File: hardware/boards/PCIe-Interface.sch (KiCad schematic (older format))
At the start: 1 part, among them U1 ECP5UM5G-381caBGA

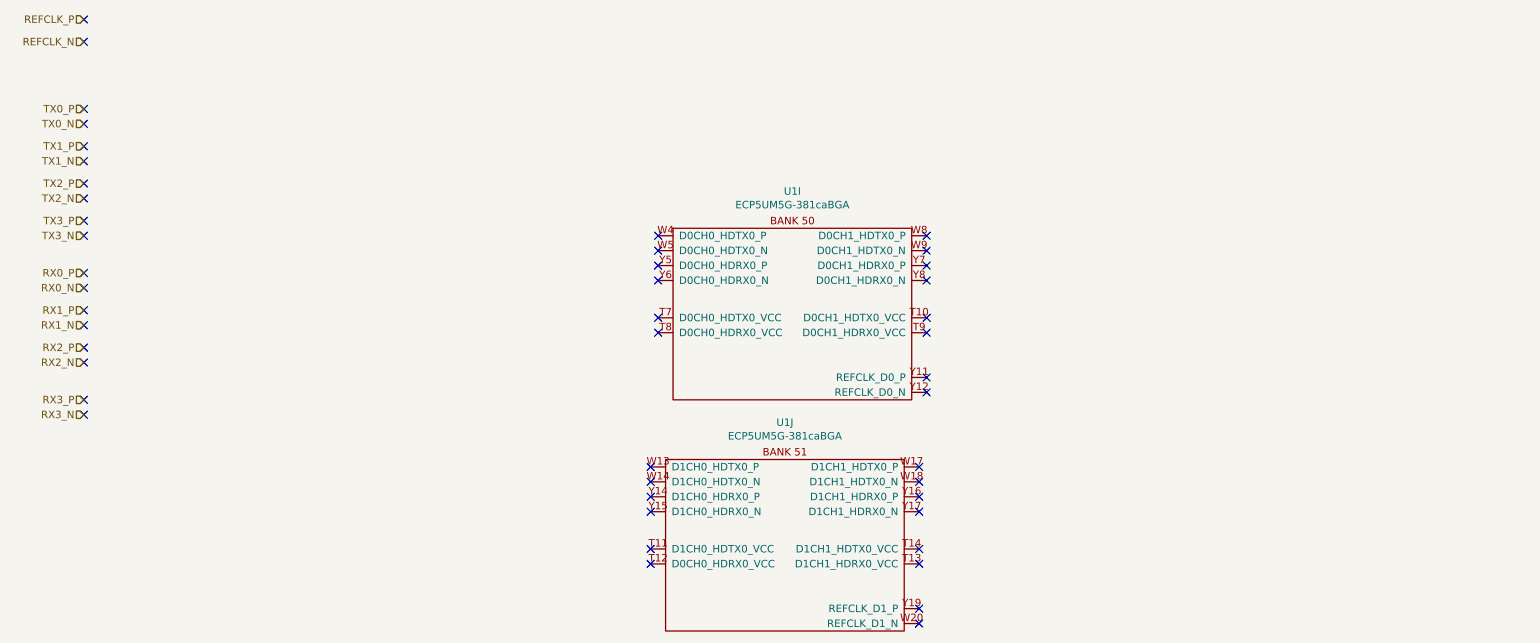
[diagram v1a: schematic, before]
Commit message: Added a clock fanout buffer for the PCIe REFCLOCK to connect to the FPGAs SERDES banks
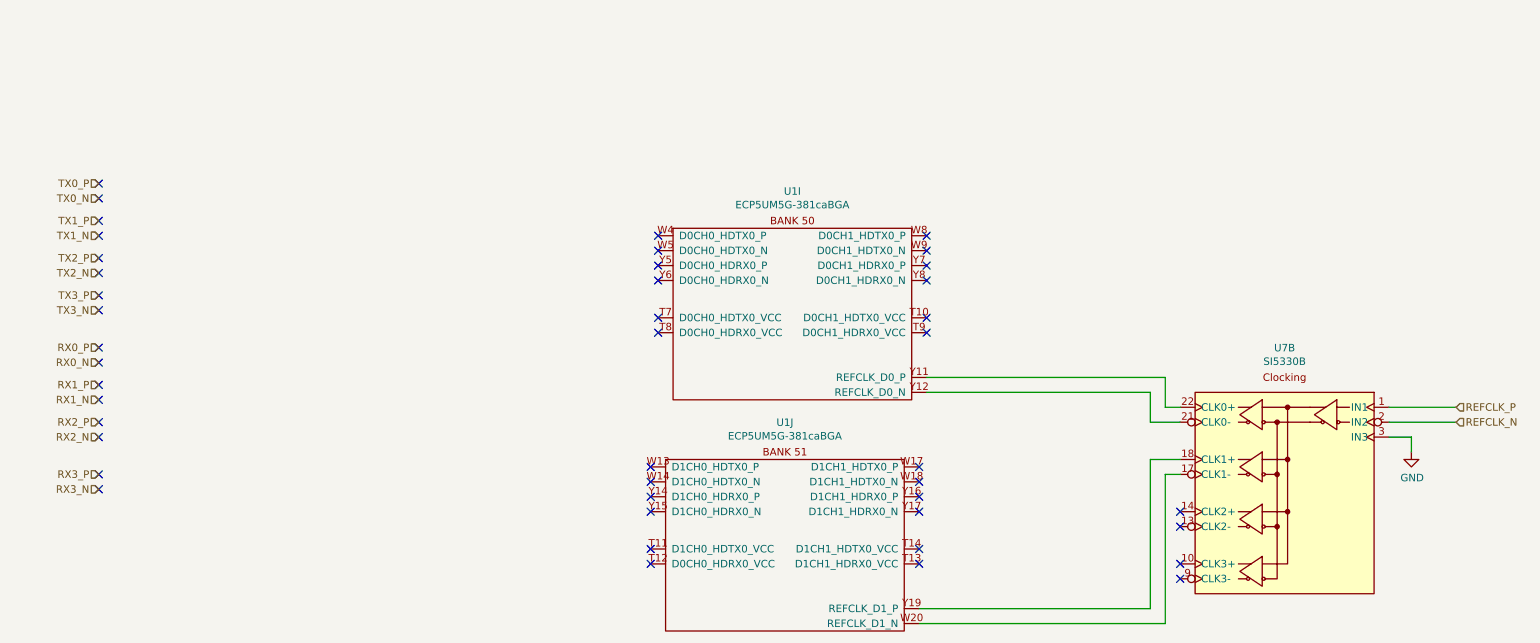
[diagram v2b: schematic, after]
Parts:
- added U7: SI5330B, Package_DFN_QFN:VQFN-24-1EP_4x4mm_P0.5mm_EP2.45x2.45mm, symbol lethalbit:SI5330B
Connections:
- net REFCLK_N: now also U7.2 (IN2)
- net REFCLK_P: now also U7.1 (IN1)
- net at U1.Y11 (REFCLK_D0_P): now also U7.22 (CLK0+)
- net at U1.Y12 (REFCLK_D0_N): now also U7.21 (CLK0-)
- net at U1.W20 (REFCLK_D1_N): now also U7.17 (CLK1-)
- net at U1.Y19 (REFCLK_D1_P): now also U7.18 (CLK1+)
- new net GND: U7.3 (IN3)
- no-connect marks 46 -> 44
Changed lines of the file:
@@
 Comment4 ""
 $EndDescr
-Text HLabel 1300 800  0    50   Input ~ 0
+Text HLabel 10500 3400 2    50   Input ~ 0
 REFCLK_P
-Text HLabel 1300 950  0    50   Input ~ 0
+Text HLabel 10500 3500 2    50   Input ~ 0
 REFCLK_N
-Text HLabel 1300 1400 0    50   Input ~ 0
+Text HLabel 1400 1900 0    50   Input ~ 0
 TX0_P
-Text HLabel 1300 1500 0    50   Input ~ 0
+Text HLabel 1400 2000 0    50   Input ~ 0
 TX0_N
-Text HLabel 1300 1650 0    50   Input ~ 0
+Text HLabel 1400 2150 0    50   Input ~ 0
 TX1_P
-Text HLabel 1300 1750 0    50   Input ~ 0
+Text HLabel 1400 2250 0    50   Input ~ 0
 TX1_N
-Text HLabel 1300 1900 0    50   Input ~ 0
+Text HLabel 1400 2400 0    50   Input ~ 0
 TX2_P
-Text HLabel 1300 2000 0    50   Input ~ 0
+Text HLabel 1400 2500 0    50   Input ~ 0
 TX2_N
-Text HLabel 1300 2150 0    50   Input ~ 0
+Text HLabel 1400 2650 0    50   Input ~ 0
 TX3_P
-Text HLabel 1300 2250 0    50   Input ~ 0
+Text HLabel 1400 2750 0    50   Input ~ 0
 TX3_N
-Text HLabel 1300 2500 0    50   Input ~ 0
+Text HLabel 1400 3000 0    50   Input ~ 0
 RX0_P
-Text HLabel 1300 2600 0    50   Input ~ 0
+Text HLabel 1400 3100 0    50   Input ~ 0
 RX0_N
-Text HLabel 1300 2750 0    50   Input ~ 0
+Text HLabel 1400 3250 0    50   Input ~ 0
 RX1_P
-Text HLabel 1300 2850 0    50   Input ~ 0
+Text HLabel 1400 3350 0    50   Input ~ 0
 RX1_N
-Text HLabel 1300 3000 0    50   Input ~ 0
+Text HLabel 1400 3500 0    50   Input ~ 0
 RX2_P
-Text HLabel 1300 3100 0    50   Input ~ 0
+Text HLabel 1400 3600 0    50   Input ~ 0
 RX2_N
-Text HLabel 1300 3350 0    50   Input ~ 0
+Text HLabel 1400 3850 0    50   Input ~ 0
 RX3_P
-Text HLabel 1300 3450 0    50   Input ~ 0
+Text HLabel 1400 3950 0    50   Input ~ 0
 RX3_N
 $Comp
@@
 	1    0    0    -1
 $EndComp
-NoConn ~ 1300 800
-NoConn ~ 1300 950
-NoConn ~ 1300 1400
-NoConn ~ 1300 1500
-NoConn ~ 1300 1650
-NoConn ~ 1300 1750
-NoConn ~ 1300 1900
-NoConn ~ 1300 2000
-NoConn ~ 1300 2150
-NoConn ~ 1300 2250
-NoConn ~ 1300 2500
-NoConn ~ 1300 2600
-NoConn ~ 1300 2750
-NoConn ~ 1300 2850
-NoConn ~ 1300 3000
-NoConn ~ 1300 3100
-NoConn ~ 1300 3350
-NoConn ~ 1300 3450
+NoConn ~ 1400 1900
+NoConn ~ 1400 2000
+NoConn ~ 1400 2150
+NoConn ~ 1400 2250
+NoConn ~ 1400 2400
+NoConn ~ 1400 2500
+NoConn ~ 1400 2650
+NoConn ~ 1400 2750
+NoConn ~ 1400 3000
+NoConn ~ 1400 3100
+NoConn ~ 1400 3250
+NoConn ~ 1400 3350
+NoConn ~ 1400 3500
+NoConn ~ 1400 3600
+NoConn ~ 1400 3850
+NoConn ~ 1400 3950
 NoConn ~ 5150 2250
 NoConn ~ 5150 2350
@@
 NoConn ~ 6900 4350
 NoConn ~ 6900 4450
-NoConn ~ 6900 4750
-NoConn ~ 6900 4850
-NoConn ~ 6950 3300
-NoConn ~ 6950 3200
 NoConn ~ 6950 2900
 NoConn ~ 6950 2800
@@
 NoConn ~ 6950 2350
 NoConn ~ 6950 2250
+$Comp
+L lethalbit:SI5330B U7
+U 2 1 5F1A1842
+P 9350 3400
+F 0 "U7" H 9350 3798 50  0000 C CNN
+F 1 "SI5330B" H 9350 3707 50  0000 C CNN
+F 2 "Package_DFN_QFN:VQFN-24-1EP_4x4mm_P0.5mm_EP2.45x2.45mm" H 9350 3700 50  0001 C CNN
+F 3 "https://www.silabs.com/documents/public/data-sheets/Si5330.pdf" H 9350 3700 50  0001 C CNN
+F 4 "Silicon Labs" H 9350 3400 50  0001 C CNN "MFR"
+F 5 "SI5330B-B00205-GM" H 9350 3400 50  0001 C CNN "MPN"
+	2    9350 3400
+	-1   0    0    -1
+$EndComp
+Wire Wire Line
+	10050 3400 10500 3400
+Wire Wire Line
+	10050 3500 10500 3500
+$Comp
+L power:GND #PWR0142
+U 1 1 5F1DBF37
+P 10200 3700
+F 0 "#PWR0142" H 10200 3450 50  0001 C CNN
+F 1 "GND" H 10205 3527 50  0000 C CNN
+F 2 "" H 10200 3700 50  0001 C CNN
+F 3 "" H 10200 3700 50  0001 C CNN
+	1    10200 3700
+	1    0    0    -1
+$EndComp
+Wire Wire Line
+	10050 3600 10200 3600
+Wire Wire Line
+	10200 3600 10200 3700
+NoConn ~ 8650 4100
+NoConn ~ 8650 4200
+NoConn ~ 8650 4450
+NoConn ~ 8650 4550
+Wire Wire Line
+	8650 3400 8550 3400
+Wire Wire Line
+	8550 3400 8550 3200
+Wire Wire Line
+	8550 3200 6950 3200
+Wire Wire Line
+	8650 3500 8450 3500
+Wire Wire Line
+	8450 3500 8450 3300
+Wire Wire Line
+	8450 3300 6950 3300
+Wire Wire Line
+	6900 4750 8450 4750
+Wire Wire Line
+	8450 4750 8450 3750
+Wire Wire Line
+	8450 3750 8650 3750
+Wire Wire Line
+	6900 4850 8550 4850
+Wire Wire Line
+	8550 4850 8550 3850
+Wire Wire Line
+	8550 3850 8650 3850
 $EndSCHEMATC

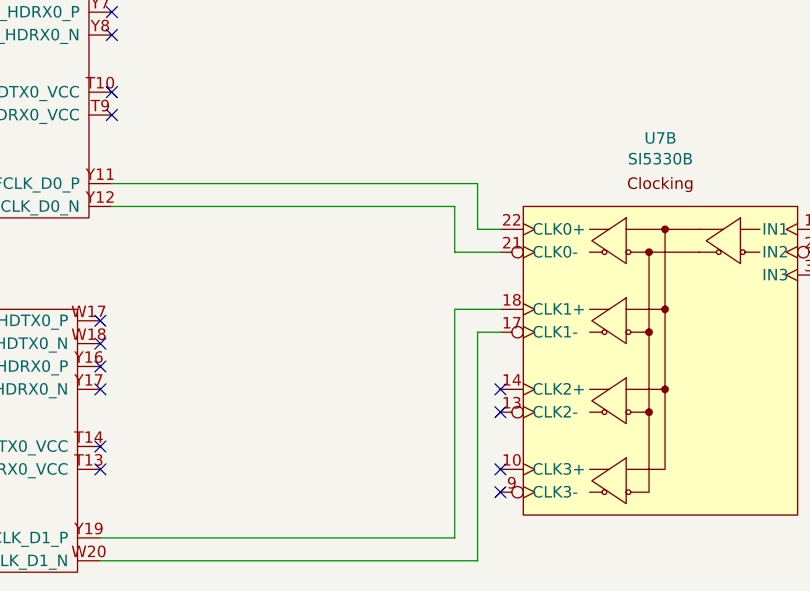
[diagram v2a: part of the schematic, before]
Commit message: Named the diff-pair clock nets
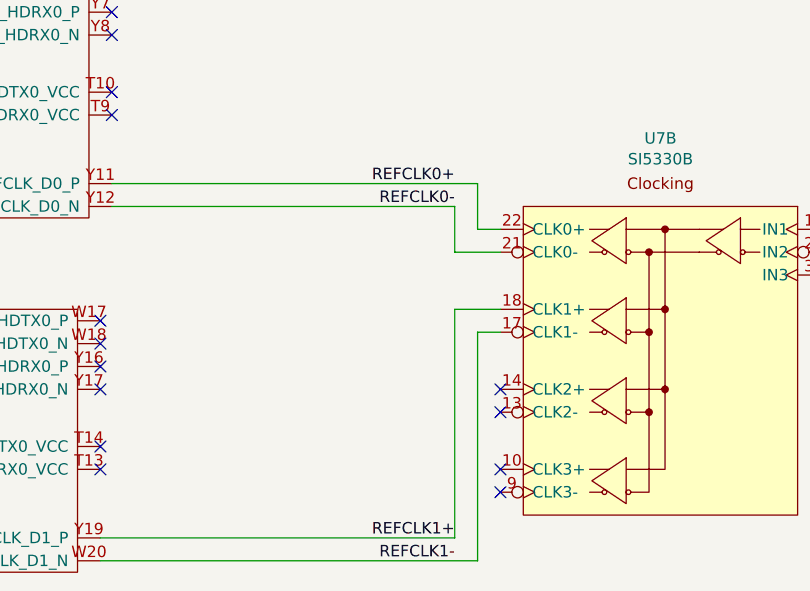
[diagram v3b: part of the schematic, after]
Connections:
- net REFCLK0+: now reaches U1.Y11 (REFCLK_D0_P), U7.22 (CLK0+)
- net REFCLK0-: now reaches U1.Y12 (REFCLK_D0_N), U7.21 (CLK0-)
- net REFCLK1-: now reaches U1.W20 (REFCLK_D1_N), U7.17 (CLK1-)
- net REFCLK1+: now reaches U1.Y19 (REFCLK_D1_P), U7.18 (CLK1+)
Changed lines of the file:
@@
 Wire Wire Line
 	8550 3850 8650 3850
+Text Label 8450 3200 2    50   ~ 0
+REFCLK0+
+Text Label 8450 3300 2    50   ~ 0
+REFCLK0-
+Text Label 8450 4750 2    50   ~ 0
+REFCLK1+
+Text Label 8450 4850 2    50   ~ 0
+REFCLK1-
 $EndSCHEMATC

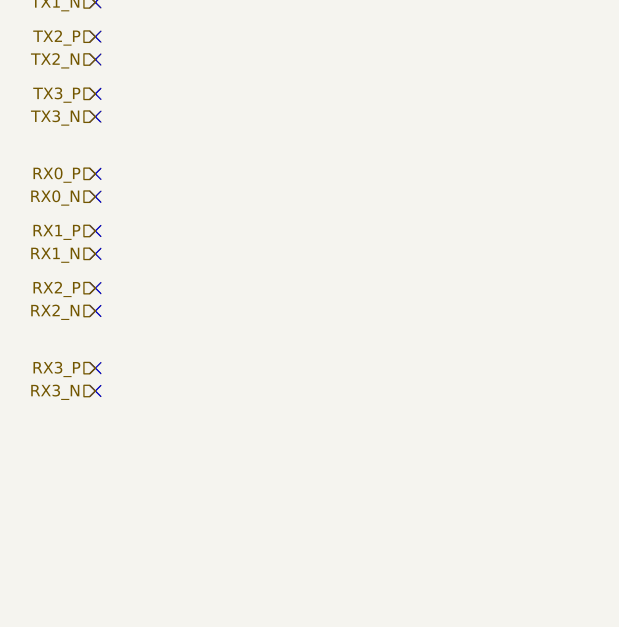
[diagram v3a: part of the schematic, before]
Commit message: Added missing bypass caps for the VCCO rails for the clock buffer
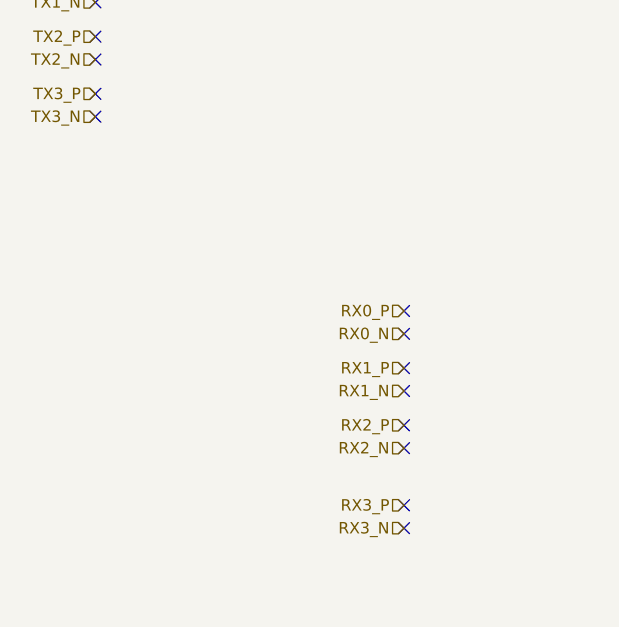
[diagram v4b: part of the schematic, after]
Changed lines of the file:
@@
 Text HLabel 1400 2750 0    50   Input ~ 0
 TX3_N
-Text HLabel 1400 3000 0    50   Input ~ 0
+Text HLabel 2750 3600 0    50   Input ~ 0
 RX0_P
-Text HLabel 1400 3100 0    50   Input ~ 0
+Text HLabel 2750 3700 0    50   Input ~ 0
 RX0_N
-Text HLabel 1400 3250 0    50   Input ~ 0
+Text HLabel 2750 3850 0    50   Input ~ 0
 RX1_P
-Text HLabel 1400 3350 0    50   Input ~ 0
+Text HLabel 2750 3950 0    50   Input ~ 0
 RX1_N
-Text HLabel 1400 3500 0    50   Input ~ 0
+Text HLabel 2750 4100 0    50   Input ~ 0
 RX2_P
-Text HLabel 1400 3600 0    50   Input ~ 0
+Text HLabel 2750 4200 0    50   Input ~ 0
 RX2_N
-Text HLabel 1400 3850 0    50   Input ~ 0
+Text HLabel 2750 4450 0    50   Input ~ 0
 RX3_P
-Text HLabel 1400 3950 0    50   Input ~ 0
+Text HLabel 2750 4550 0    50   Input ~ 0
 RX3_N
 $Comp
@@
 NoConn ~ 1400 2650
 NoConn ~ 1400 2750
-NoConn ~ 1400 3000
-NoConn ~ 1400 3100
-NoConn ~ 1400 3250
-NoConn ~ 1400 3350
-NoConn ~ 1400 3500
-NoConn ~ 1400 3600
-NoConn ~ 1400 3850
-NoConn ~ 1400 3950
+NoConn ~ 2750 3600
+NoConn ~ 2750 3700
+NoConn ~ 2750 3850
+NoConn ~ 2750 3950
+NoConn ~ 2750 4100
+NoConn ~ 2750 4200
+NoConn ~ 2750 4450
+NoConn ~ 2750 4550
 NoConn ~ 5150 2250
 NoConn ~ 5150 2350

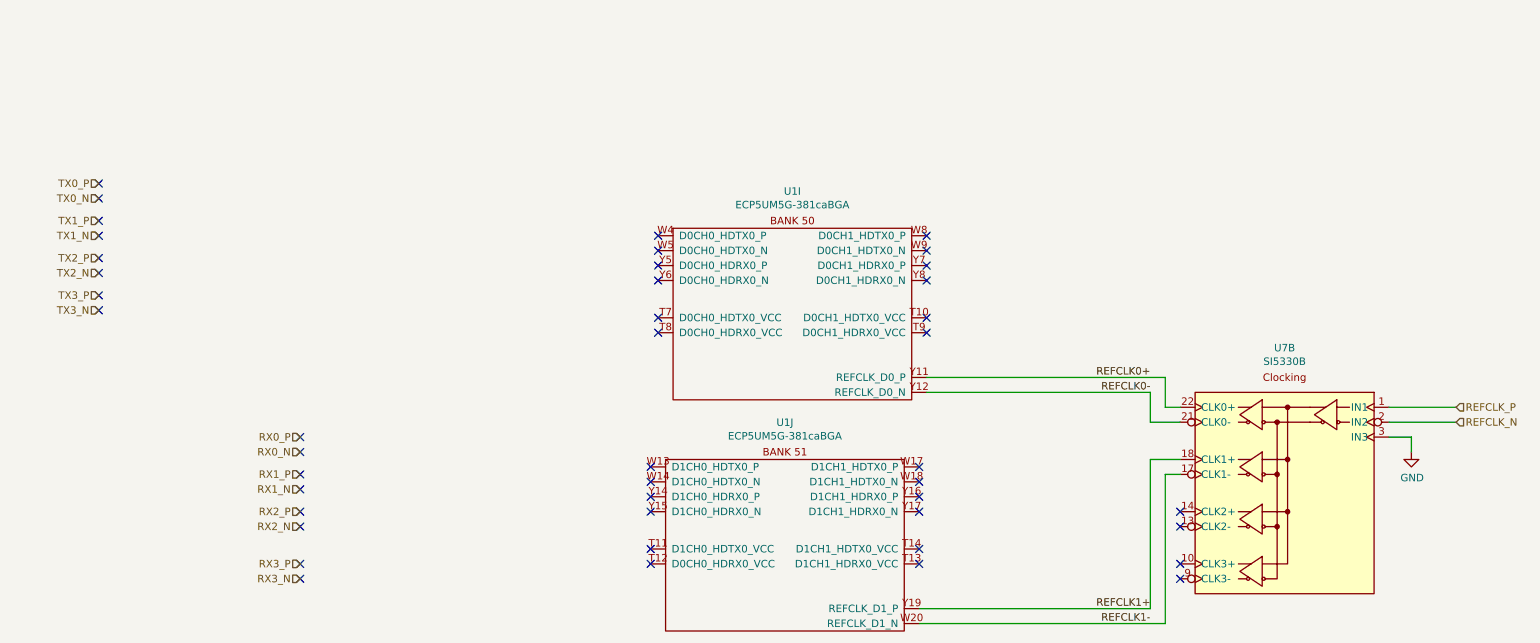
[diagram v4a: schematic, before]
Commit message: Connected the PCIe lanes to the FPGA SERDES channels
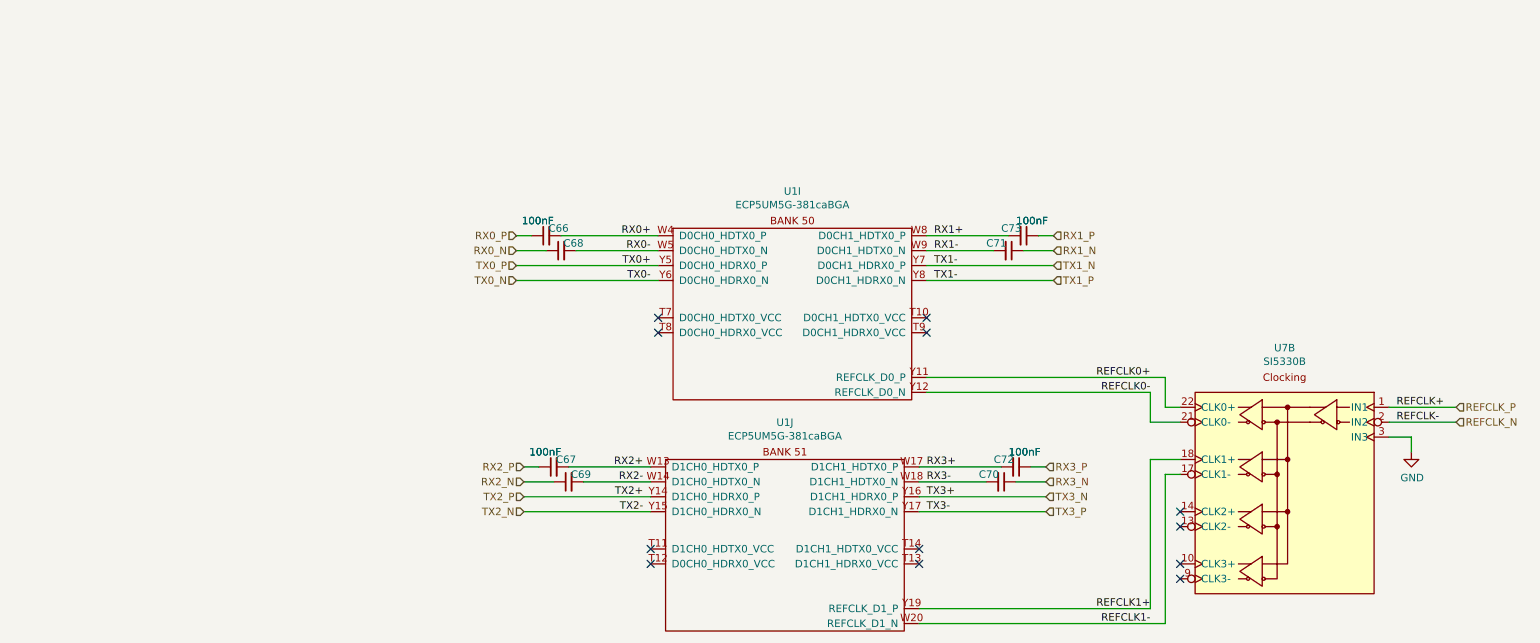
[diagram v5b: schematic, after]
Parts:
- added C66, C67, C68, C69, C70, C71, C72, C73: 100nF, Capacitor_SMD:C_0402_1005Metric, symbol Device:C_Small
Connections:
- net RX0_N: now also C68.1
- net RX0_P: now also C66.1
- net RX1_N: now also C71.1
- net RX1_P: now also C73.1
- net RX2_N: now also C69.1
- net RX2_P: now also C67.1
- net RX3_N: now also C70.1
- net RX3_P: now also C72.1
- net TX0_N: now also U1.Y6 (D0CH0_HDRX0_N)
- net TX0_P: now also U1.Y5 (D0CH0_HDRX0_P)
- net TX1_N: now also U1.Y7 (D0CH1_HDRX0_P), U1.Y8 (D0CH1_HDRX0_N)
- net TX2_N: now also U1.Y15 (D1CH0_HDRX0_N)
- net TX2_P: now also U1.Y14 (D1CH0_HDRX0_P)
- net TX3_N: now also U1.Y16 (D1CH1_HDRX0_P)
- net TX3_P: now also U1.Y17 (D1CH1_HDRX0_N)
- net RX0+: now reaches U1.W4 (D0CH0_HDTX0_P)
- net RX0+: now also C66.2
- net RX0-: now reaches U1.W5 (D0CH0_HDTX0_N)
- net RX0-: now also C68.2
- net RX1+: now reaches U1.W8 (D0CH1_HDTX0_P)
- net RX1+: now also C73.2
- net RX1-: now reaches U1.W9 (D0CH1_HDTX0_N)
- net RX1-: now also C71.2
- net RX2+: now reaches U1.W13 (D1CH0_HDTX0_P)
- net RX2+: now also C67.2
- net RX2-: now reaches U1.W14 (D1CH0_HDTX0_N)
- net RX2-: now also C69.2
- net RX3+: now reaches U1.W17 (D1CH1_HDTX0_P)
- net RX3+: now also C72.2
- net RX3-: now reaches U1.W18 (D1CH1_HDTX0_N)
- net RX3-: now also C70.2
- no-connect marks 44 -> 12
